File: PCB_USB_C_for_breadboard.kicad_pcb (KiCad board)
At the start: 2 copper layers, 23.6 x 18 mm, 14 parts, among them J1 USB_C_Receptacle_USB2.0_16P, J2 Conn_01x02_Pin, J3 Conn_01x02_Pin, J4 Conn_01x03_Pin, J5 Conn_01x05_Socket, SW1 SW_SPDT, U1 LM1117GS-3.3

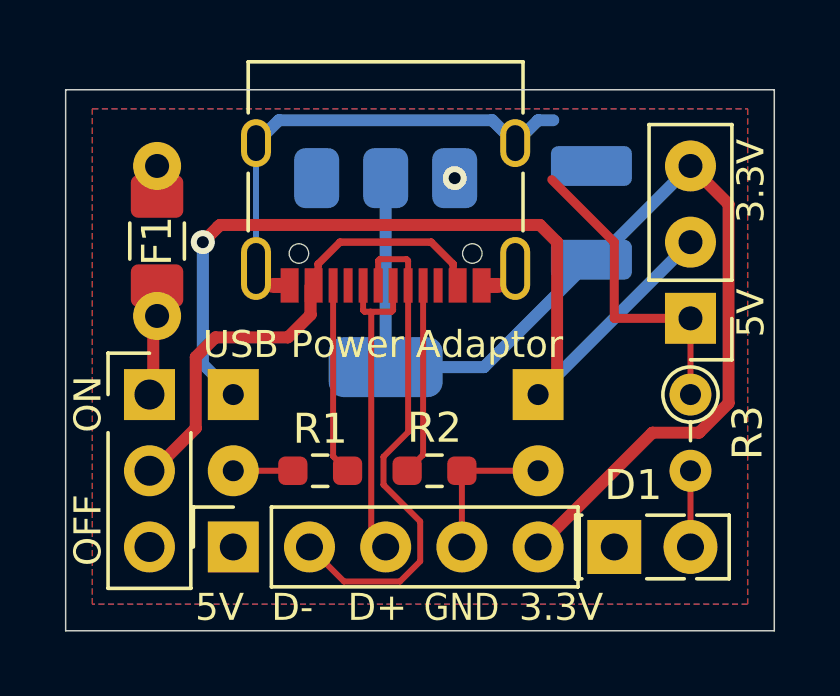
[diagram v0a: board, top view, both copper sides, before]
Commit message: Adjust SW1 position
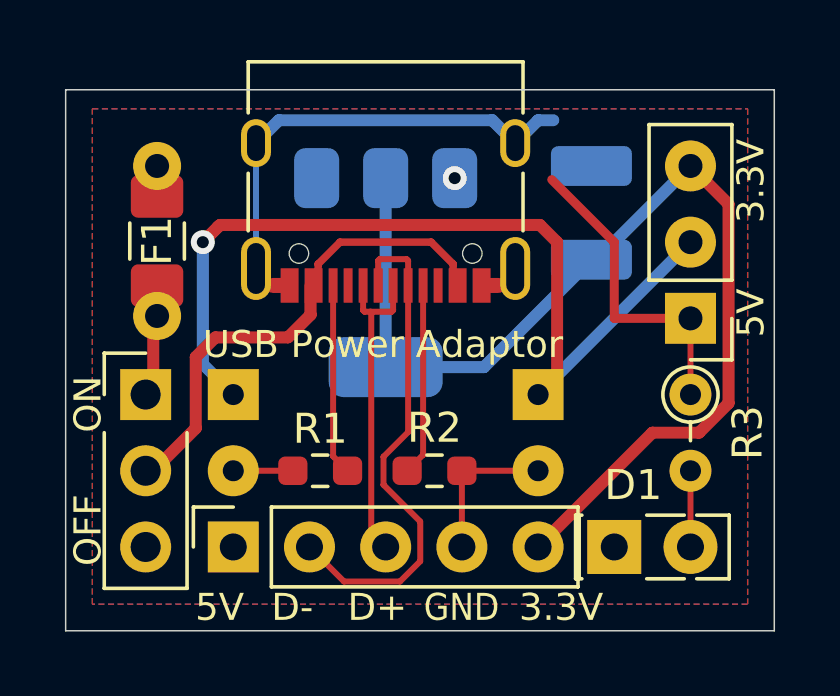
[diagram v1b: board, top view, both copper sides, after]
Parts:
- moved SW1 0.13 mm to (91.1, 38.1)
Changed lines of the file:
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@@
 	(footprint "Connector_PinHeader_2.54mm:PinHeader_1x03_P2.54mm_Vertical"
 		(layer "F.Cu")
-		(at 91.186 38.1)
+		(at 91.059 38.1)
 		(descr "Through hole straight pin header, 1x03, 2.54mm pitch, single row")
 		(tags "Through hole pin header THT 1x03 2.54mm single row")

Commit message: Rev. 4
Shrink PCB size.
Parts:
- moved C1 10.6 mm to (99.0, 40.1), turned to 180 degrees
- moved J4 2.62 mm to (106.9, 34.3)
- moved R3 2.62 mm to (106.9, 36.8)
- moved D1 0.68 mm to (106.9, 43.8), turned to 90 degrees
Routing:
- net +5V: track 10.6 -> 0.00 mm
- net +3.3V: track 38.8 -> 30.2 mm
- net GND: track 25.6 -> 27.6 mm
- net Net-(D1-A): track 2.54 -> 1.91 mm
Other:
- board size 23.6 x 18 mm -> 21.3 x 18 mm
- board text added: "+"
- board text added: "-"
- board text removed: "VDD"
